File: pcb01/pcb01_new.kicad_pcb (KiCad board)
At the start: 2 copper layers, 119.4 x 91.4 mm, 59 parts, among them J1 DIN41612_02x32_AC, J11 Conn_01x09, J2 Jmp_UART_Irq, J3 Conn_01x09_Socket, J4 Conn_01x08_Socket, J5 UART, J6 Conn_01x02_Socket, J7 Jmp_Irq, J8 Jmp_NMI, J9 Ram1 Enable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

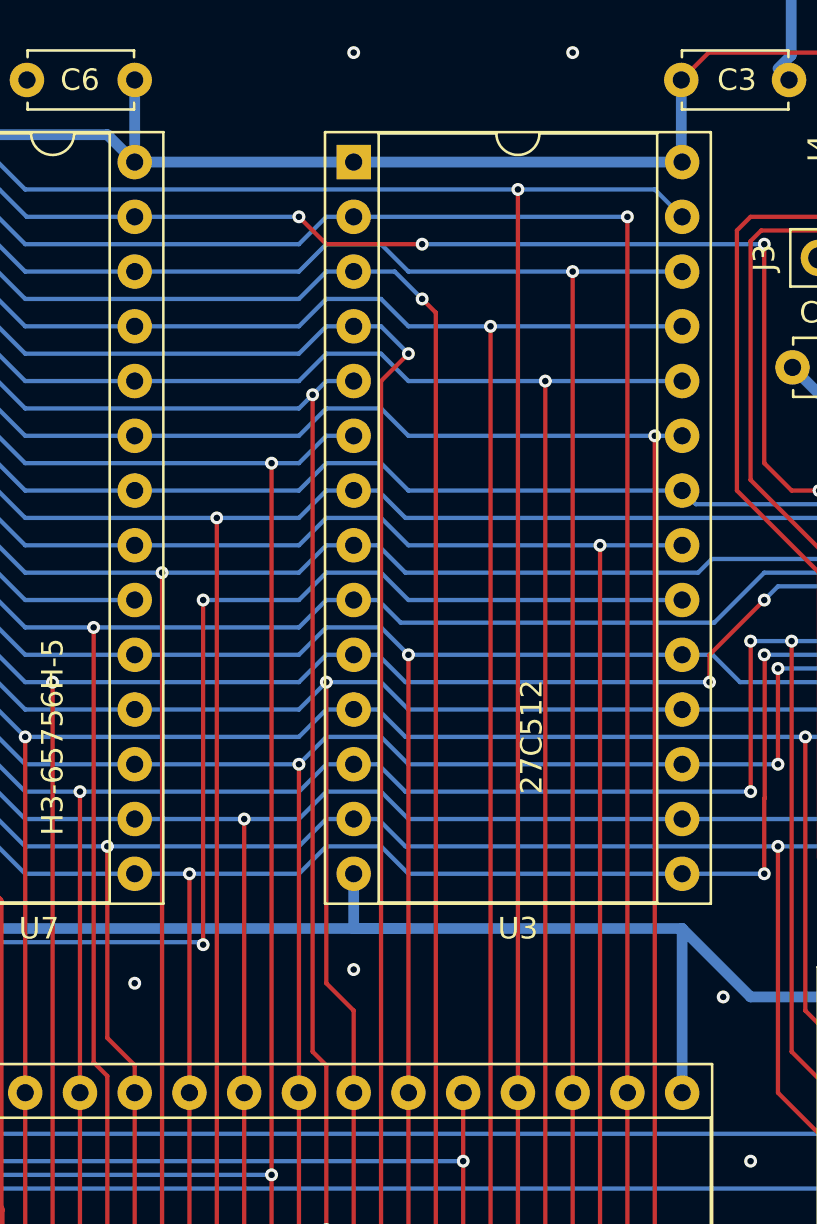
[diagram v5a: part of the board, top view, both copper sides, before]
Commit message: connect rom A15
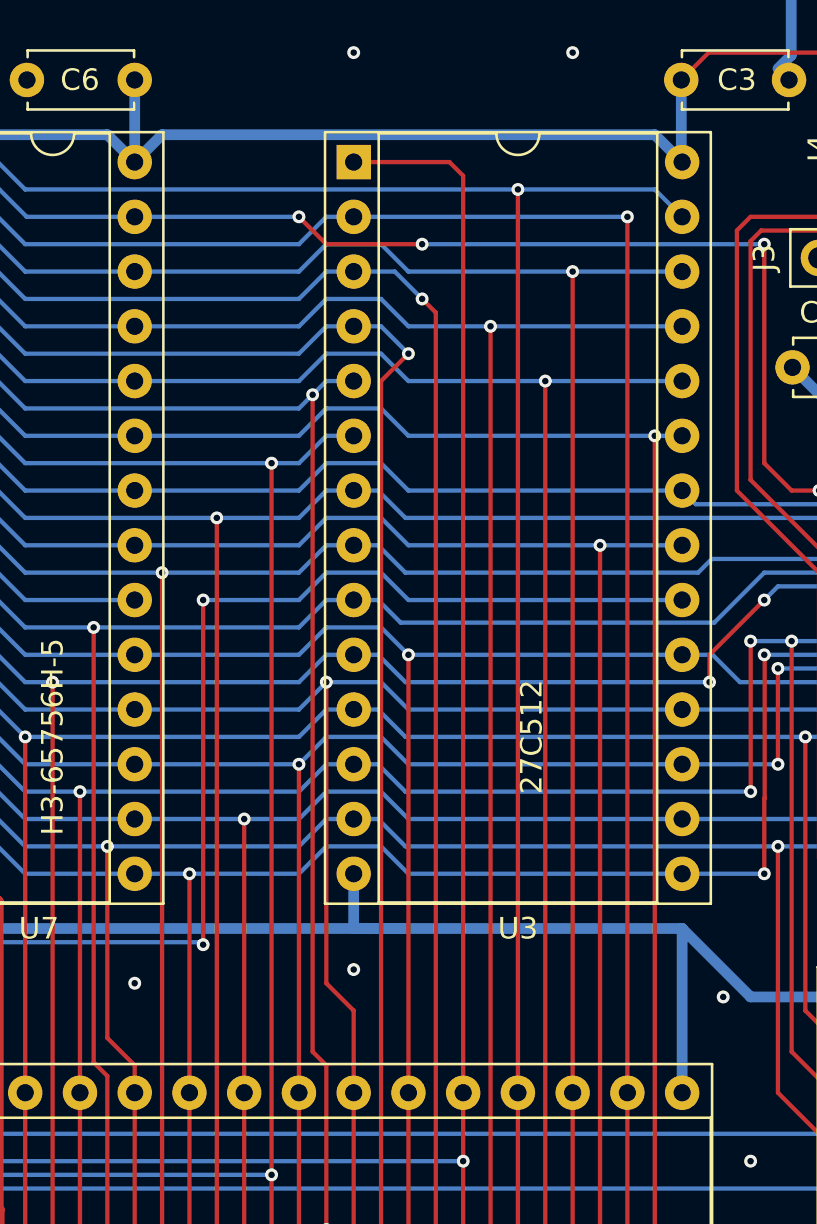
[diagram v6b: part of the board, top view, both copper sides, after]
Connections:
- U3 pad 1: VCC -> /A15
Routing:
- net /A15: track 124.1 -> 172.0 mm
- net VCC: track 540.5 -> 541.5 mm
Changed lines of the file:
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@@
       (stroke (width 0.1) (type solid)) (layer "F.Fab"))
     (pad "1" thru_hole rect (at 0 0) (size 1.6 1.6) (drill 0.8) (layers "*.Cu" "*.Mask")
-      (net 2 "VCC") (pinfunction "A15") (pintype "input"))
+      (net 66 "/A15") (pinfunction "A15") (pintype "input"))
     (pad "2" thru_hole oval (at 0 2.54) (size 1.6 1.6) (drill 0.8) (layers "*.Cu" "*.Mask")
       (net 19 "/A12") (pinfunction "A12") (pintype "input"))
@@
   (segment (start 121.285 43.18) (end 121.92 42.545) (width 0.2) (layer "B.Cu") (net 2))
   (segment (start 63.5 83.82) (end 64.77 82.55) (width 0.2) (layer "B.Cu") (net 2))
+  (segment (start 83.82 25.4) (end 85.09 24.13) (width 0.5) (layer "B.Cu") (net 2))
   (segment (start 64.77 82.55) (end 77.47 82.55) (width 0.2) (layer "B.Cu") (net 2))
   (segment (start 54.61 24.13) (end 67.31 24.13) (width 0.5) (layer "B.Cu") (net 2))
@@
   (segment (start 83.82 21.59) (end 83.82 25.4) (width 0.5) (layer "B.Cu") (net 2))
   (segment (start 67.31 24.13) (end 68.58 25.4) (width 0.5) (layer "B.Cu") (net 2))
+  (segment (start 85.09 24.13) (end 107.95 24.13) (width 0.5) (layer "B.Cu") (net 2))
   (segment (start 68.58 21.59) (end 68.58 25.4) (width 0.5) (layer "B.Cu") (net 2))
   (segment (start 53.34 25.4) (end 54.61 24.13) (width 0.5) (layer "B.Cu") (net 2))
+  (segment (start 107.95 24.13) (end 109.22 25.4) (width 0.5) (layer "B.Cu") (net 2))
   (segment (start 53.34 21.4) (end 53.34 25.4) (width 0.5) (layer "B.Cu") (net 2))
   (segment (start 68.58 25.4) (end 69.85 24.13) (width 0.5) (layer "B.Cu") (net 2))
-  (segment (start 83.82 25.4) (end 109.22 25.4) (width 0.5) (layer "B.Cu") (net 2))
   (segment (start 77.47 82.55) (end 78.74 83.82) (width 0.2) (layer "B.Cu") (net 2))
   (segment (start 82.55 99.06) (end 83.82 100.33) (width 0.2) (layer "F.Cu") (net 7))
@@
   (segment (start 100.33 82.55) (end 99.06 81.28) (width 0.2) (layer "F.Cu") (net 66))
   (segment (start 55.245 70.485) (end 55.245 57.15) (width 0.2) (layer "F.Cu") (net 66))
+  (segment (start 99.06 68.58) (end 99.06 26.035) (width 0.2) (layer "F.Cu") (net 66))
   (segment (start 100.33 85.725) (end 100.33 82.55) (width 0.2) (layer "F.Cu") (net 66))
   (segment (start 99.06 68.58) (end 99.06 71.755) (width 0.2) (layer "F.Cu") (net 66))
+  (segment (start 98.425 25.4) (end 93.98 25.4) (width 0.2) (layer "F.Cu") (net 66))
   (segment (start 55.88 71.12) (end 55.245 70.485) (width 0.2) (layer "F.Cu") (net 66))
   (segment (start 99.06 81.28) (end 99.06 71.755) (width 0.2) (layer "F.Cu") (net 66))
+  (segment (start 99.06 26.035) (end 98.425 25.4) (width 0.2) (layer "F.Cu") (net 66))
   (segment (start 99.06 86.995) (end 100.33 85.725) (width 0.2) (layer "F.Cu") (net 66))
   (via (at 55.88 71.12) (size 0.6) (drill 0.3) (layers "F.Cu" "B.Cu") (net 66))

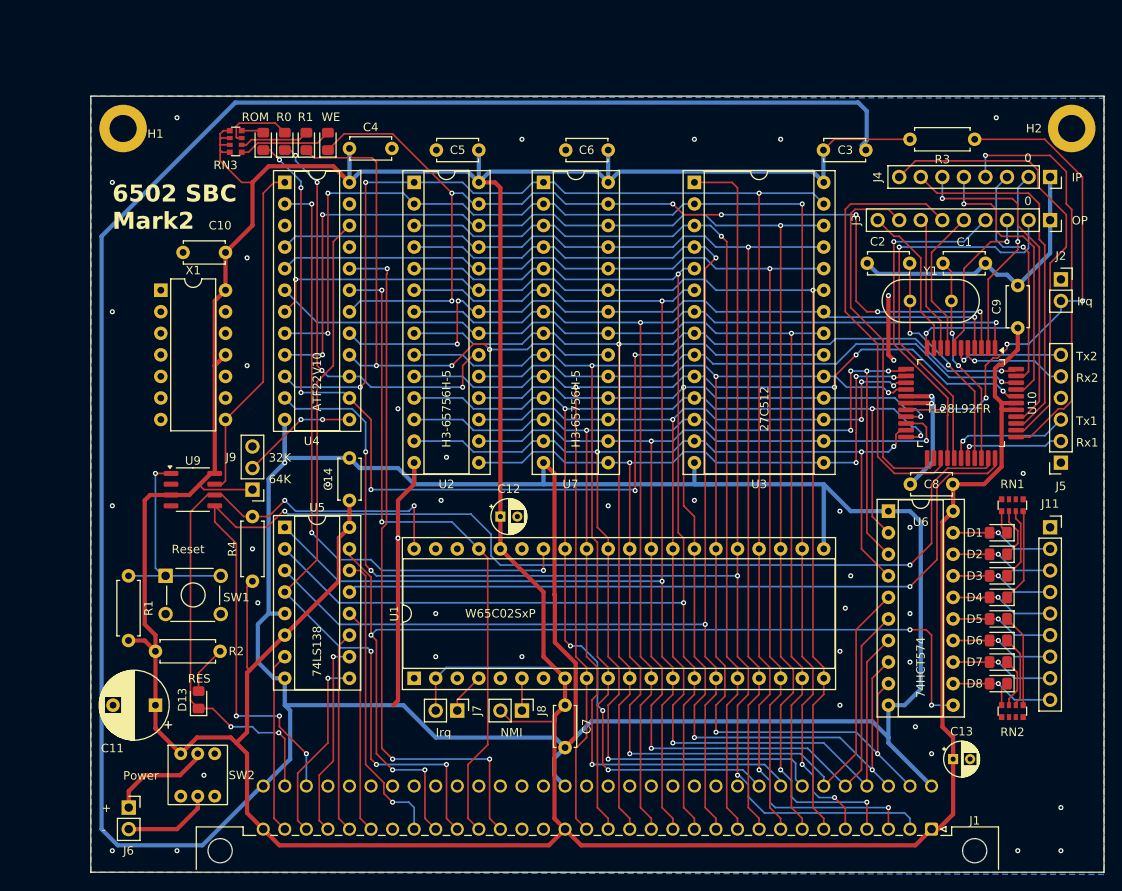
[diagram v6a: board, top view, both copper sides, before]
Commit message: big pld reorder & break out unused pins
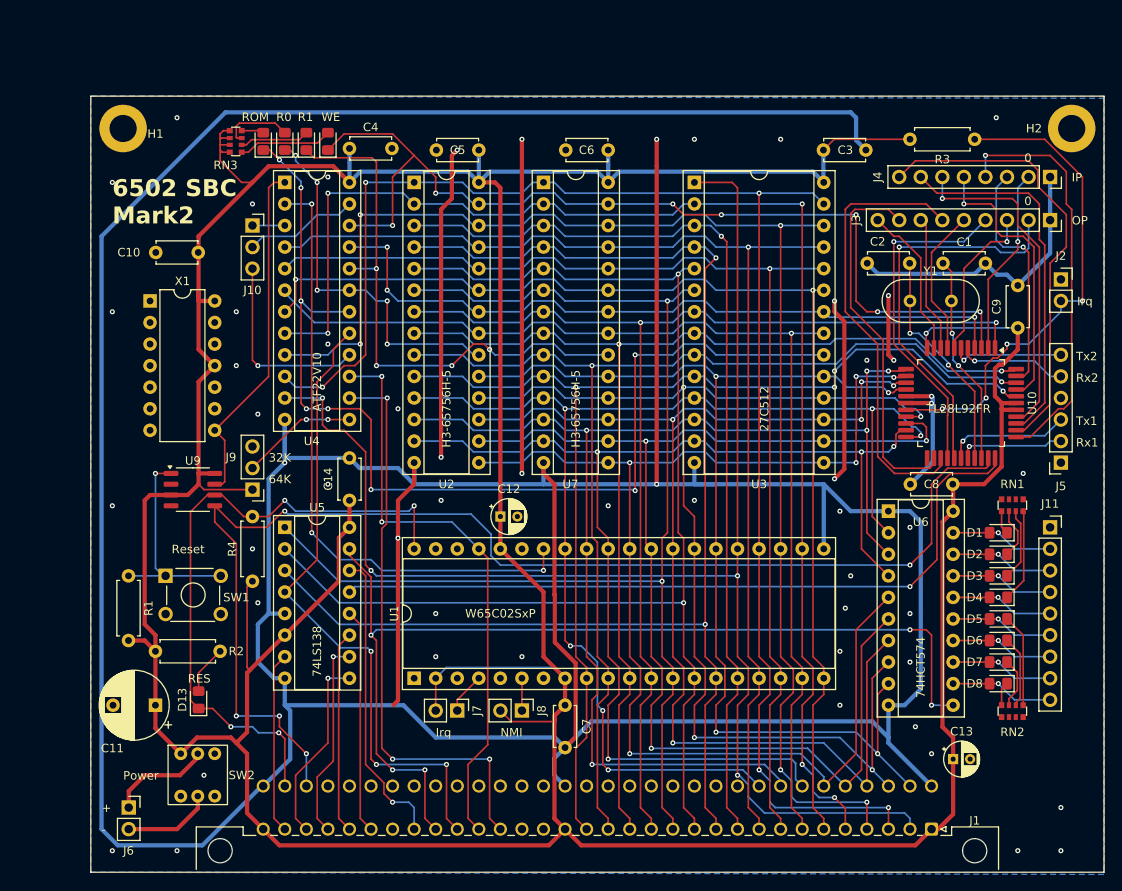
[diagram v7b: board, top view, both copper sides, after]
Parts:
- added J10: PLD_aux, Connector_PinSocket_2.54mm:PinSocket_1x03_P2.54mm_Vertical, F.Cu at (41.9, 30.5)
- moved C10 3.21 mm to (35.5, 33.7)
- moved X1 1.80 mm to (29.8, 39.4)
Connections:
- U4 pad 14: /~{CS_ROM} -> /~{SYS_CLK}
- U4 pad 15: /~{CS_RAM0} -> /SYS_CLK
- U4 pad 16: /~{CS_RAM1} -> /PLD_O7
- U4 pad 17: /~{QOE} -> /~{IO_SEL}
- U4 pad 18: /~{QWE_RAM} -> /~{CS_ROM}
- U4 pad 19: /SYS_CLK -> /~{CS_RAM0}
- U4 pad 20: /~{SYS_CLK} -> /~{CS_RAM1}
- U4 pad 21: unconnected-(U4-O2-Pad21) -> /~{QOE}
- U4 pad 22: /~{IO_SEL} -> /~{QWE_RAM}
- U4 pad 23: unconnected-(U4-O0-Pad23) -> /PLD_O0
- U4 pad 3: unconnected-(U4-I1-Pad3) -> /PLD_I1
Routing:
- net GND: track 584.5 -> 720.7 mm, vias 44 -> 55
- net /PLD_O7: track 0.00 -> 23.0 mm, vias 0 -> 1
- net /~{SYS_CLK}: track 83.2 -> 68.0 mm
- net /PLD_O0: track 0.00 -> 13.5 mm
- net /~{IO_SEL}: track 89.4 -> 76.7 mm
- net /SYS_CLK: track 78.8 -> 68.6 mm
- net /~{QWE_RAM}: track 122.9 -> 113.2 mm
- net /D1: track 154.1 -> 147.1 mm, vias 6 -> 5
- net /~{CS_ROM}: track 119.1 -> 126.1 mm, vias 6 -> 8
- net /~{CS_RAM0}: track 50.5 -> 44.3 mm, vias 4 -> 5
- net VCC: track 541.5 -> 546.1 mm
- net /PLD_I1: track 0.00 -> 3.81 mm
- net /A14: track 180.0 -> 178.1 mm
- net /CLOCK: track 40.2 -> 41.2 mm
- net /A13: track 164.0 -> 163.3 mm
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
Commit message: mostly change resistors & caps to smd
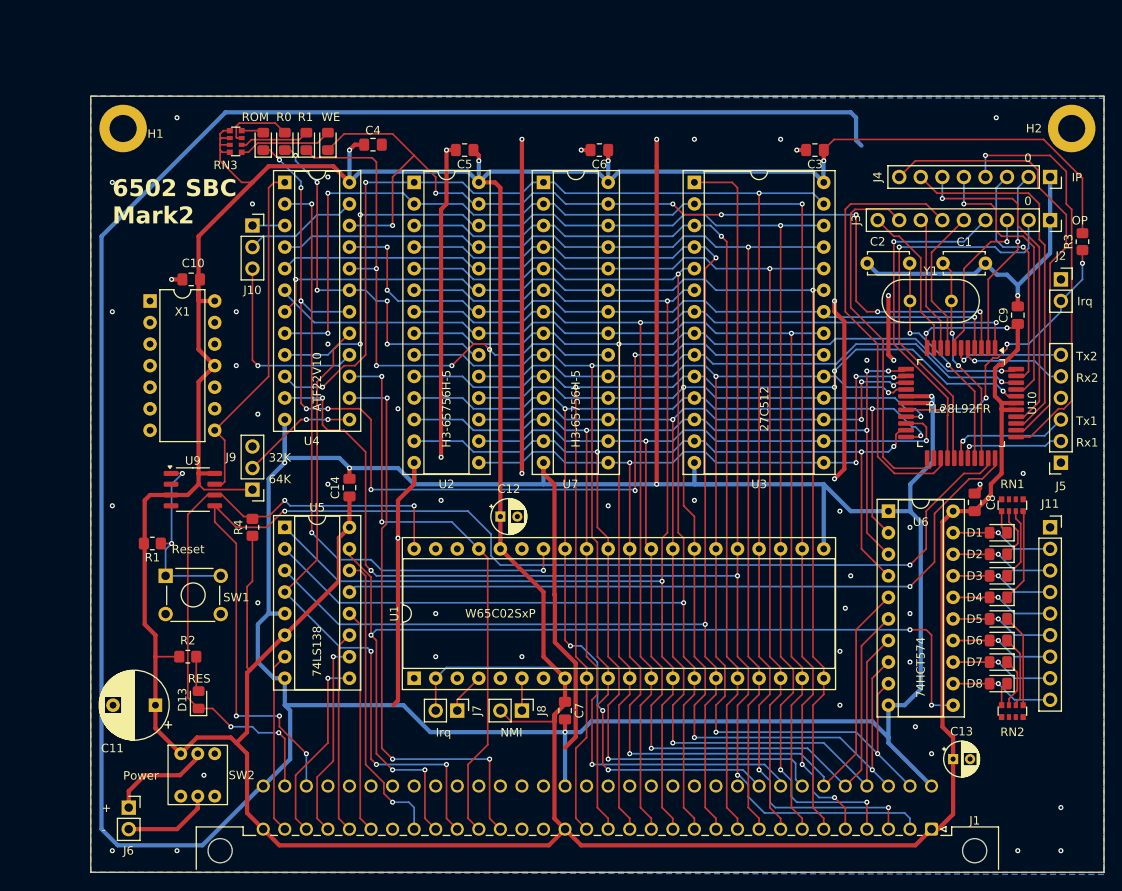
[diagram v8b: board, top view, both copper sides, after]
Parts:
- C10, C14, C3, C4, C5, C6, C7, C8, C9: footprint Capacitor_THT:C_Disc_D4.7mm_W2.5mm_P5.00mm -> Capacitor_SMD:C_0805_2012Metric_Pad1.18x1.45mm_HandSolder
- R1, R2, R3, R4: footprint Resistor_THT:R_Axial_DIN0207_L6.3mm_D2.5mm_P7.62mm_Horizontal -> Resistor_SMD:R_0805_2012Metric_Pad1.20x1.40mm_HandSolder
- moved R3 17.5 mm to (139.7, 32.4), turned to 90 degrees
- moved R4 6.35 mm to (41.9, 66.0)
- moved R1 4.73 mm to (30.1, 67.9), turned to 180 degrees
- moved R2 3.86 mm to (34.3, 81.3)
- moved C8 3.35 mm to (127.0, 63.1), turned to 90 degrees
- moved C10 3.28 mm to (34.7, 36.8)
- moved C4 2.81 mm to (56.1, 21.0)
- moved C5 1.67 mm to (66.9, 21.6)
- moved C14 1.50 mm to (53.3, 61.4)
- moved C9 1.50 mm to (132.1, 41.0)
- moved C6 1.04 mm to (82.8, 21.6)
- moved C3 1.00 mm to (108.2, 21.6), turned to 180 degrees
- moved C7 0.63 mm to (78.7, 87.6)
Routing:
- net VCC: track 546.1 -> 581.2 mm, vias 1 -> 6
- net /~{IRQ_UART}: track 58.7 -> 34.0 mm
- net GND: track 720.7 -> 733.8 mm, vias 55 -> 61
- net Net-(U9-~{PB_RST}): track 25.9 -> 22.9 mm, vias 1 -> 2
- net /~{IOEN_02_UART}: track 88.2 -> 86.5 mm
- net Net-(D13-A): track 5.74 -> 4.17 mm
- net /RES: track 147.4 -> 145.9 mm
